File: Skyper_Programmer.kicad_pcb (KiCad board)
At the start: 2 copper layers, 23 x 16 mm, 32 parts, among them IC1 MAX232, J1 Pager, J10 Pin9, J11 Pin5, J2 USB PWR, J3 Pin1, J4 Pin6, J5 Pin2, J6 Pin7, J7 Pin3, J8 Pin8, J9 Pin4, T1 BC847, T2 BC847, U1 TC1055

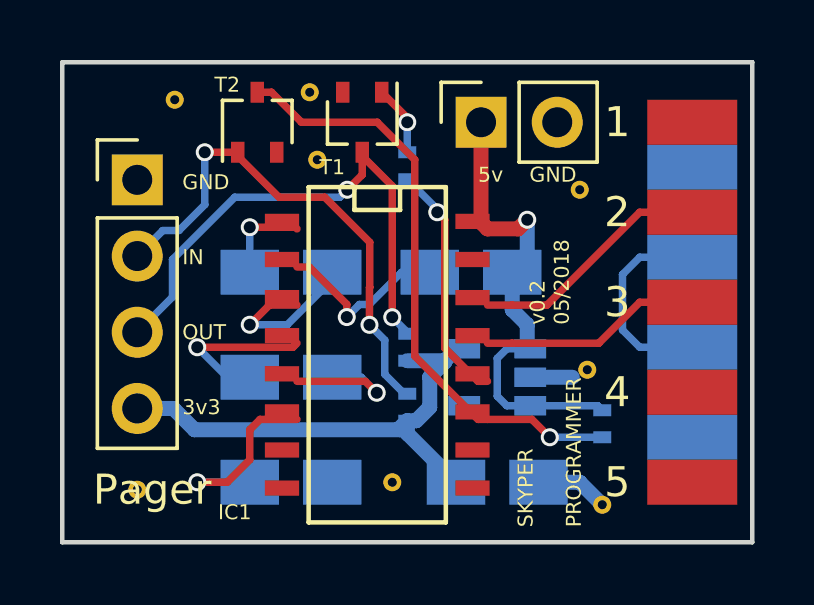
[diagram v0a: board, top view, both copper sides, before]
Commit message: Change pin header labelling
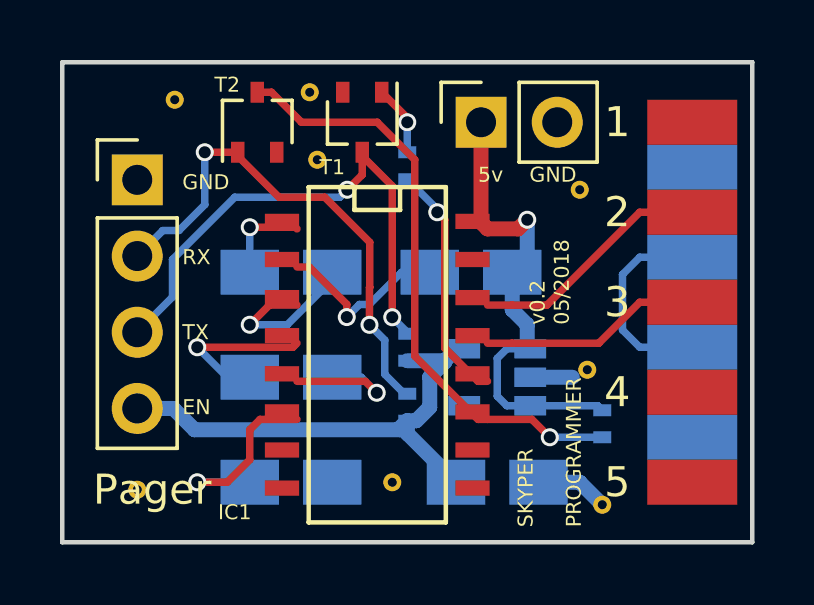
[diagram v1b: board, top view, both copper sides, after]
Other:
- board text added: "EN"
- board text added: "RX"
- board text added: "TX"
- board text removed: "3v3"
- board text removed: "IN"
- board text removed: "OUT"
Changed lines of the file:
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@@
-(kicad_pcb (version 20171130) (host pcbnew 5.0.0-rc2-dev-unknown-538ab0e~65~ubuntu18.04.1)
+(kicad_pcb (version 20171130) (host pcbnew 5.0.0-rc3-unknown-101b68b~65~ubuntu18.04.1)
   (general
     (thickness 1.6)
@@
   (title_block
     (title SKYPER_PROGRAMMER)
-    (date 2018-05-21)
+    (date 2018-07-10)
     (rev v0.2)
     (company "J. Putzger, DF2ET, DK4PA")
@@
       (hpglpennumber 1)
       (hpglpenspeed 20)
-      (hpglpendiameter 15)
+      (hpglpendiameter 15.000000)
       (psnegative false)
       (psa4output false)
@@
     (effects (font (size 0.5 0.5) (thickness 0.125)))
   )
-  (gr_text 3v3 (at 140 82.5) (layer F.SilkS)
+  (gr_text EN (at 140 82.5) (layer F.SilkS)
     (effects (font (size 0.5 0.5) (thickness 0.125)) (justify left))
   )
-  (gr_text OUT (at 140 80) (layer F.SilkS)
+  (gr_text TX (at 140 80) (layer F.SilkS)
     (effects (font (size 0.5 0.5) (thickness 0.125)) (justify left))
   )
-  (gr_text IN (at 140 77.5) (layer F.SilkS)
+  (gr_text RX (at 140 77.5) (layer F.SilkS)
     (effects (font (size 0.5 0.5) (thickness 0.125)) (justify left))
   )

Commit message: Update pic and meta data
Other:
- board text added: "v0.2 07/2018"
- board text removed: "v0.2 05/2018"
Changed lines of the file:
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@@
-(kicad_pcb (version 20171130) (host pcbnew 5.0.0-rc3-unknown-101b68b~65~ubuntu18.04.1)
+(kicad_pcb (version 20171130) (host pcbnew 5.0.0-rc3-unknown-14ce5182~65~ubuntu18.04.1)
   (general
     (thickness 1.6)
@@
   (title_block
     (title SKYPER_PROGRAMMER)
-    (date 2018-07-10)
+    (date 2018-07-11)
     (rev v0.2)
     (company "J. Putzger, DF2ET, DK4PA")
@@
     (effects (font (size 0.5 0.5) (thickness 0.125)) (justify left mirror))
   )
-  (gr_text "v0.2\n05/2018" (at 152.25 79.75 90) (layer F.SilkS)
+  (gr_text "v0.2\n07/2018" (at 152.25 79.75 90) (layer F.SilkS)
     (effects (font (size 0.5 0.5) (thickness 0.125)) (justify left))
   )
